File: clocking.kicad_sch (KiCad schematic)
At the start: 38 parts, among them J9 U.Fl, U2 LMK05318BRGZR, U21 TMP117xxDRV, U3 TG5032CGN

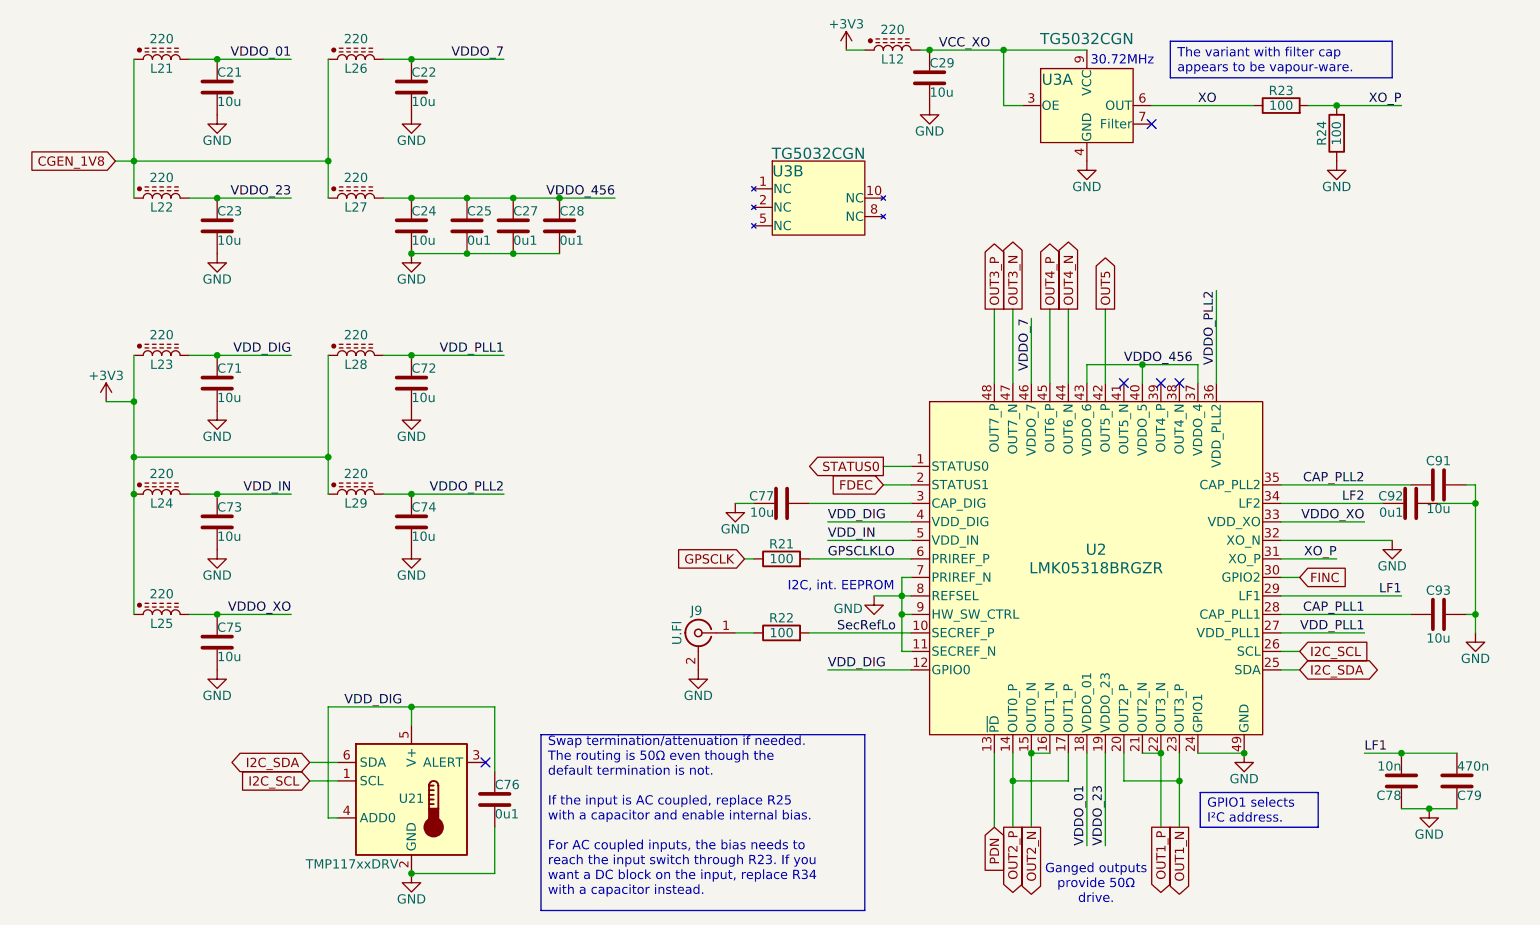
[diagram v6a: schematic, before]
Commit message: Use impedance matching baluns.
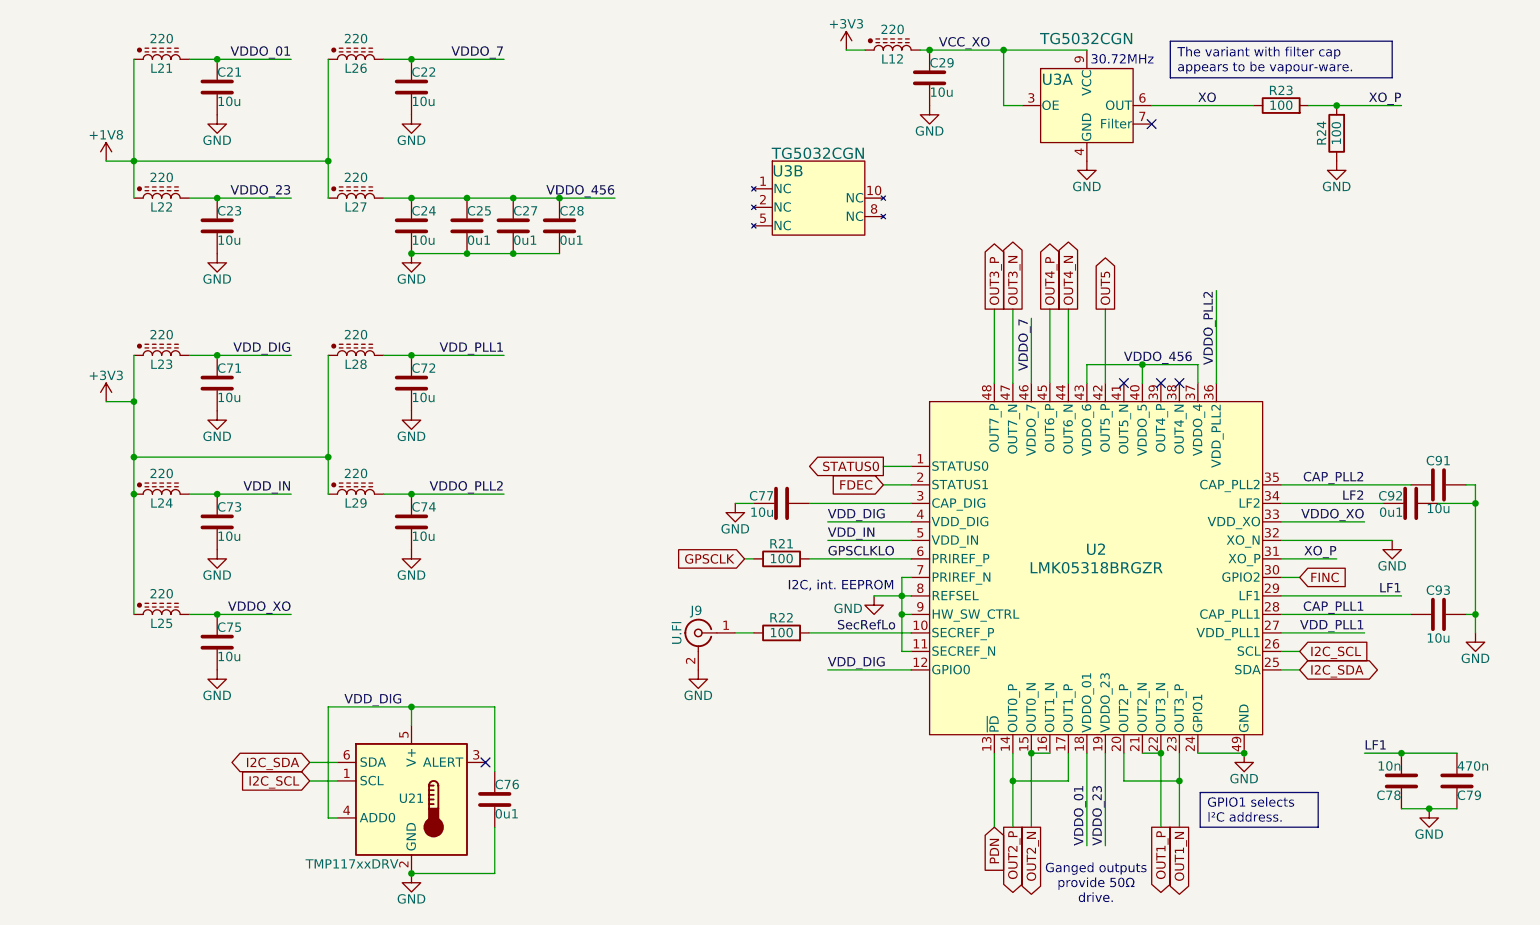
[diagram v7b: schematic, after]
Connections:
- net CGEN_1V8 renamed +1V8
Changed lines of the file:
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@@
 		)
 	)
-	(text_box "Swap termination/attenuation if needed.  The routing is 50Ω even though the default termination is not.\n\nIf the input is AC coupled, replace R25 with a capacitor and enable internal bias.\n\nFor AC coupled inputs, the bias needs to reach the input switch through R23. If you want a DC block on the input, replace R34 with a capacitor instead.\n\n"
-		(exclude_from_sim no)
-		(at 125.7299 126.9999 0)
-		(size 44.4501 24.1301)
-		(margins 0.9525 0.9525 0.9525 0.9525)
-		(stroke
-			(width 0)
-			(type solid)
-		)
-		(fill
-			(type none)
-		)
-		(effects
-			(font
-				(size 1.27 1.27)
-			)
-			(justify left)
-		)
-	)
 	(text_box "GPIO1 selects I²C address."
 		(exclude_from_sim no)
@@
 	(wire
 		(pts
-			(xy 67.31 48.26) (xy 69.85 48.26)
+			(xy 66.04 48.26) (xy 69.85 48.26)
 		)
 		(stroke
@@
 		)
 	)
-	(global_label "CGEN_1V8"
-		(shape input)
-		(at 67.31 48.26 180)
-		(fields_autoplaced yes)
-		(effects
-			(font
-				(size 1.27 1.27)
-			)
-			(justify right)
-		)
-		(property "Intersheetrefs" "${INTERSHEET_REFS}"
-			(at 54.8301 48.26 0)
-			(effects
-				(font
-					(size 1.27 1.27)
-				)
-				(justify right)
-			)
-		)
-	)
 	(global_label "FDEC"
 		(shape input)
@@
 					(unit 1)
 				)
+			)
+		)
+	)
+	(symbol
+		(lib_id "power:+1V8")
+		(at 66.04 48.26 0)
+		(unit 1)
+		(exclude_from_sim no)
+		(in_bom yes)
+		(on_board yes)
+		(dnp no)
+		(property "Reference" "#PWR062"
+			(at 66.04 52.07 0)
+			(effects
+				(font
+					(size 1.27 1.27)
+				)
+				(hide yes)
+			)
+		)
+		(property "Value" "+1V8"
+			(at 66.04 44.704 0)
+			(effects
+				(font
+					(size 1.27 1.27)
+				)
+			)
+		)
+		(property "Footprint" ""
+			(at 66.04 48.26 0)
+			(effects
+				(font
+					(size 1.27 1.27)
+				)
+				(hide yes)
+			)
+		)
+		(property "Datasheet" ""
+			(at 66.04 48.26 0)
+			(effects
+				(font
+					(size 1.27 1.27)
+				)
+				(hide yes)
+			)
+		)
+		(property "Description" "Power symbol creates a global label with name \"+1V8\""
+			(at 66.04 48.26 0)
+			(effects
+				(font
+					(size 1.27 1.27)
+				)
+				(hide yes)
+			)
+		)
+		(pin "1"
+		)
+		(instances
+			(project ""
+				(path "/3160ff17-81c2-4674-af97-e8d9acaf6b65/131a3728-0d51-4d75-9961-26d31d87be39"
+					(reference "#PWR062")
+					(unit 1)
+				)

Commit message: Routing basically done.
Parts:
- removed R22: 100, Resistor_SMD:R_0402_1005Metric, symbol Device:R
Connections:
- net SecRefLo is gone; now on net SecRef: U2.10 (SECREF_P)
- net SecRef: now reaches J9.1 (In)
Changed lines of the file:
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@@
 	(wire
 		(pts
-			(xy 162.56 113.03) (xy 176.53 113.03)
-		)
-		(stroke
-			(width 0)
-			(type default)
-		)
-	)
-	(wire
-		(pts
-			(xy 152.4 113.03) (xy 154.94 113.03)
+			(xy 152.4 113.03) (xy 176.53 113.03)
 		)
 		(stroke
@@
 		)
 	)
-	(label "SecRefLo"
-		(at 166.37 113.03 0)
+	(label "SecRef"
+		(at 165.1 113.03 0)
 		(effects
 			(font
@@
 					(unit 1)
 				)
-			)
-		)
-	)
-	(symbol
-		(lib_id "Device:R")
-		(at 158.75 113.03 90)
-		(unit 1)
-		(exclude_from_sim no)
-		(in_bom yes)
-		(on_board yes)
-		(dnp no)
-		(property "Reference" "R22"
-			(at 158.75 110.998 90)
-			(effects
-				(font
-					(size 1.27 1.27)
-				)
-			)
-		)
-		(property "Value" "100"
-			(at 158.75 113.03 90)
-			(effects
-				(font
-					(size 1.27 1.27)
-				)
-			)
-		)
-		(property "Footprint" "Resistor_SMD:R_0402_1005Metric"
-			(at 158.75 114.808 90)
-			(effects
-				(font
-					(size 1.27 1.27)
-				)
-				(hide yes)
-			)
-		)
-		(property "Datasheet" "~"
-			(at 158.75 113.03 0)
-			(effects
-				(font
-					(size 1.27 1.27)
-				)
-				(hide yes)
-			)
-		)
-		(property "Description" "Resistor"
-			(at 158.75 113.03 0)
-			(effects
-				(font
-					(size 1.27 1.27)
-				)
-				(hide yes)
-			)
-		)
-		(property "LCSC" "C25076"
-			(at 158.75 113.03 90)
-			(effects
-				(font
-					(size 1.27 1.27)
-				)
-				(hide yes)
-			)
-		)
-		(pin "2"
-		)
-		(pin "1"
-		)
-		(instances
-			(project "gpsref"
-				(path "/3160ff17-81c2-4674-af97-e8d9acaf6b65/131a3728-0d51-4d75-9961-26d31d87be39"
-					(reference "R22")
-					(unit 1)
-				)
